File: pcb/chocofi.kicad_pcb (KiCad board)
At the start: 2 copper layers, 111.3 x 90 mm, 55 parts, among them J1 MJ-4PP-9, J2 OLED, SW10 SW_PUSH, SW11 SW_PUSH, SW12 SW_PUSH, SW14 SW_PUSH, SW15 SW_PUSH, SW16 SW_PUSH, SW17 SW_PUSH, SW18 SW_PUSH, SW19 SW_PUSH, SW2 SW_PUSH, SW20 SW_PUSH, SW21 SW_PUSH, SW3 SW_PUSH, SW4 SW_PUSH, SW5 SW_PUSH, SW6 SW_PUSH, SW8 SW_PUSH, SW9 SW_PUSH, U1 ProMicro

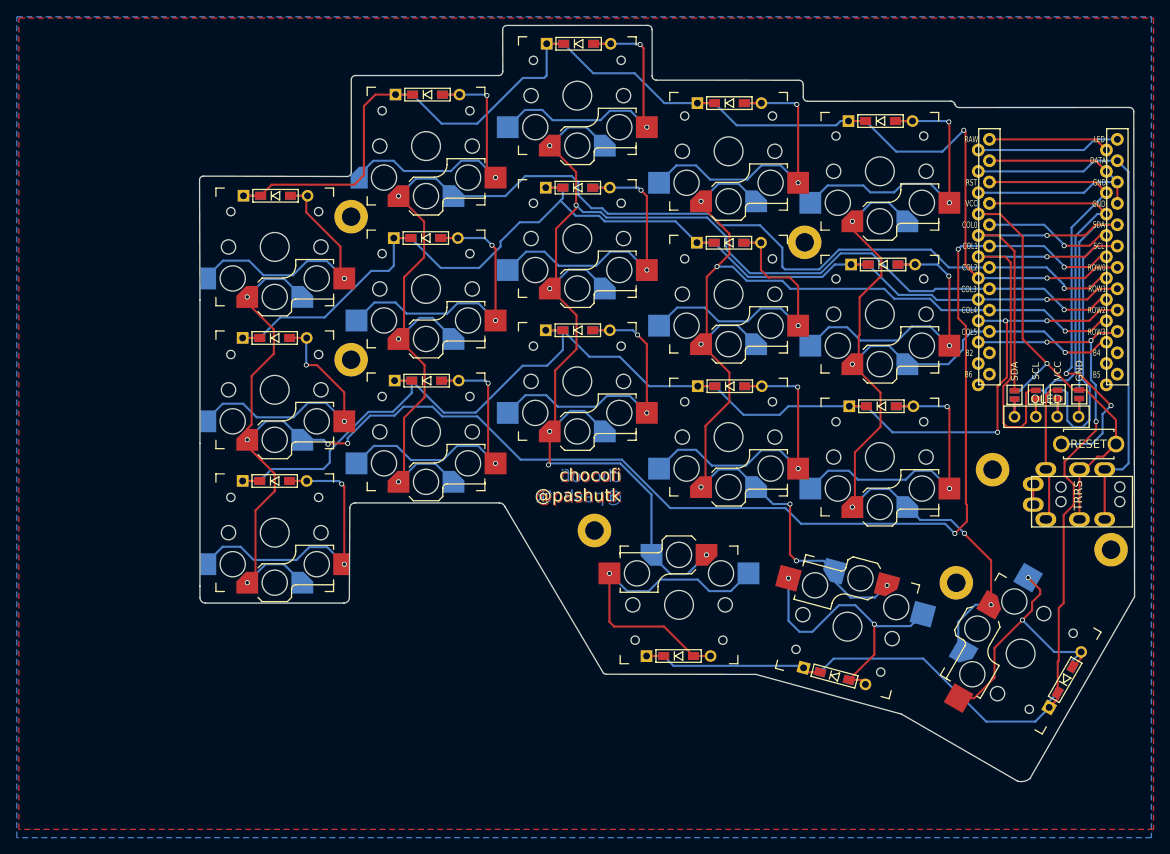
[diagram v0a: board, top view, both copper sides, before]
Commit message: Add power switch. Broken nets on scheme.
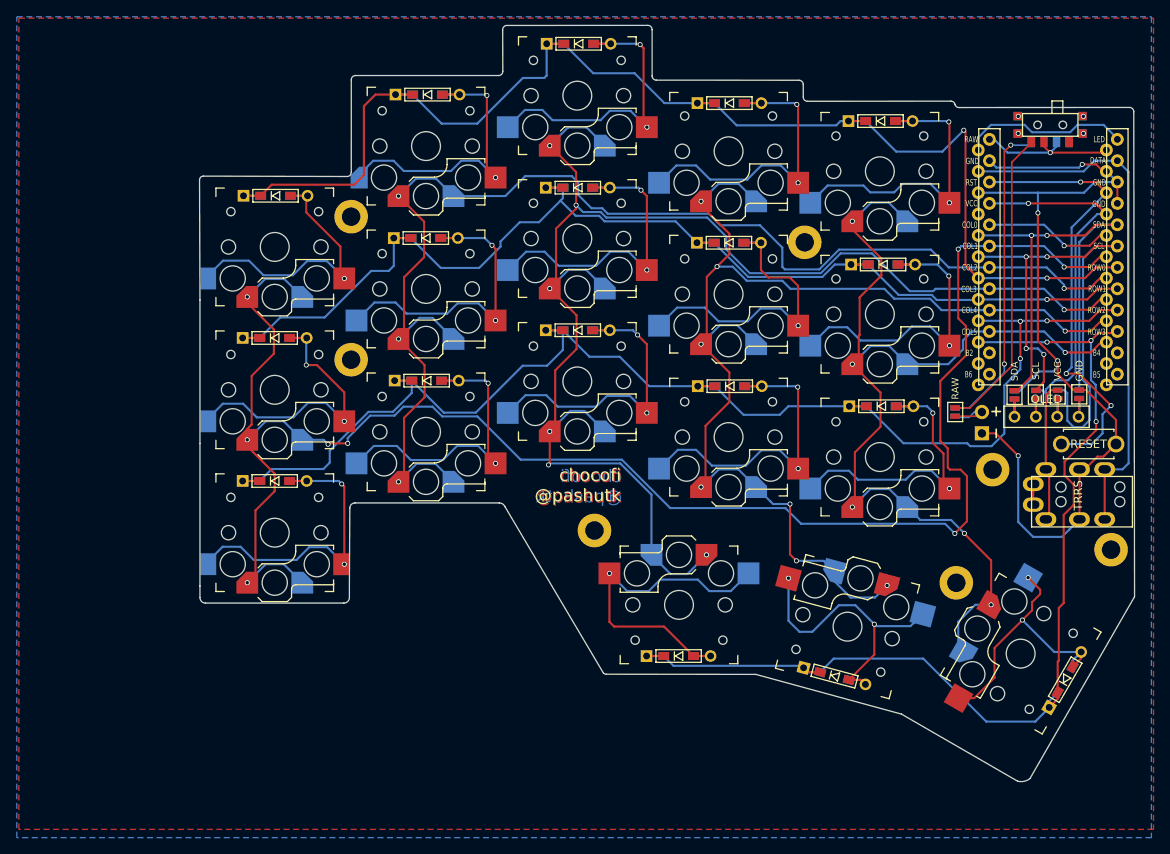
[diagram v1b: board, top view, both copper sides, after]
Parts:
- added J3: Conn_01x02_Female, kbd:Battery_TH, F.Cu at (170.1, 92.6)
- added JP61: RAW, foostan:Jumper, F.Cu at (166.9, 90.0)
- added JP62: RAW, foostan:Jumper, B.Cu at (166.9, 90.0)
- added SW1: SW_SPDT, Buttons_Switches:SW_SPDT+H-MSK12C01_hor(7pin_SMD), F.Cu at (178.2, 55.9)
- added SW2: SW_SPDT, Buttons_Switches:SW_SPDT+H-MSK12C01_hor(7pin_SMD), B.Cu at (178.2, 55.9)
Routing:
- net SW_RAW_1: track 0.00 -> 37.4 mm, vias 0 -> 2
- net SW_RAW_2: track 0.00 -> 36.1 mm
- net GND: track 91.7 -> 113.5 mm, vias 1 -> 4
- net SCL: track 80.8 -> 67.1 mm, vias 1 -> 4
- net BAT_PLUS: track 0.00 -> 5.95 mm
- net col1: track 204.9 -> 208.1 mm
- net LED: track 17.1 -> 19.8 mm
- net row2: track 154.5 -> 156.9 mm
- net Net-(U1-Pad24): track 14.4 -> 16.8 mm, vias 0 -> 1
- net SDA: track 61.7 -> 59.6 mm, vias 1 -> 2
- net Net-(D18-Pad2): track 37.2 -> 36.2 mm
- net reset: vias 2 -> 3
- net VCC: vias 0 -> 1
- net (no net): vias 0 -> 4
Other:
- board text added: "GND"

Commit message: Use thicker power trace
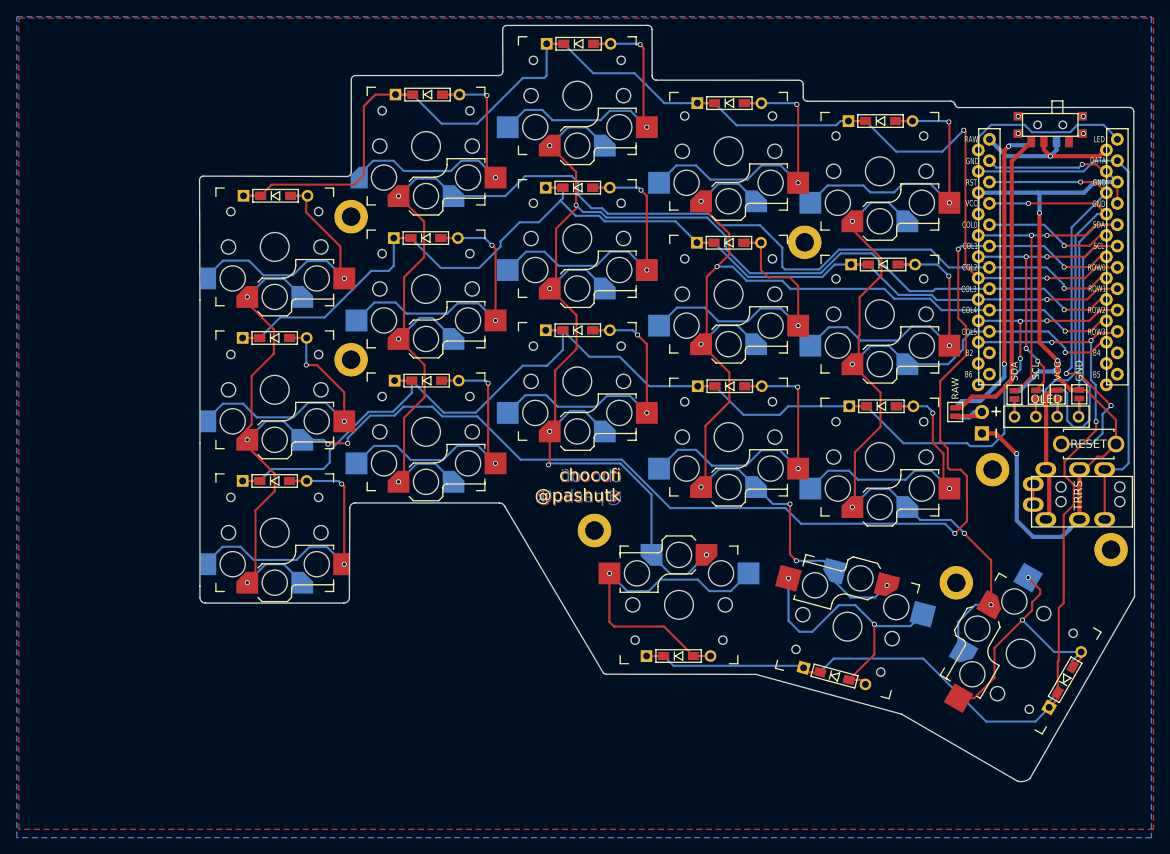
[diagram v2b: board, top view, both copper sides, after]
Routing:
- net col4: track 140.4 -> 136.4 mm
- net col5: track 118.7 -> 114.9 mm
- net col1: track 208.1 -> 205.3 mm
- net col3: track 169.9 -> 167.9 mm
- net col2: track 153.3 -> 151.4 mm
- net VCC: track 68.1 -> 66.2 mm
- net Net-(U1-Pad24): track 16.8 -> 18.5 mm
- net Net-(D18-Pad2): track 36.2 -> 34.5 mm
- net Net-(D3-Pad2): track 36.8 -> 35.3 mm
- net SW_RAW_2: track 36.1 -> 37.5 mm
- net Net-(D15-Pad2): track 37.3 -> 36.0 mm
- net Net-(D2-Pad2): track 35.5 -> 34.7 mm
- net SCL: track 67.1 -> 66.3 mm
- net BAT_PLUS: track 5.95 -> 6.57 mm
- net SW_RAW_1: track 37.4 -> 38.0 mm
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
